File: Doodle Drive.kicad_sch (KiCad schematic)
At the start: 49 parts, among them J1 USB_B, J2 PINHD_1x4_Male, J6 PINHD_1x2_Male, SW1 Push_Button, SW2 Push_Button, SW3 Push_Button, U1 STM32F411RETx, U6 AP7343-30W5-7, U7 CP2102N-Axx-xQFN28, Y1 32.768KHz ±20ppm 12.5pF, Y2 25MHZ 9PF

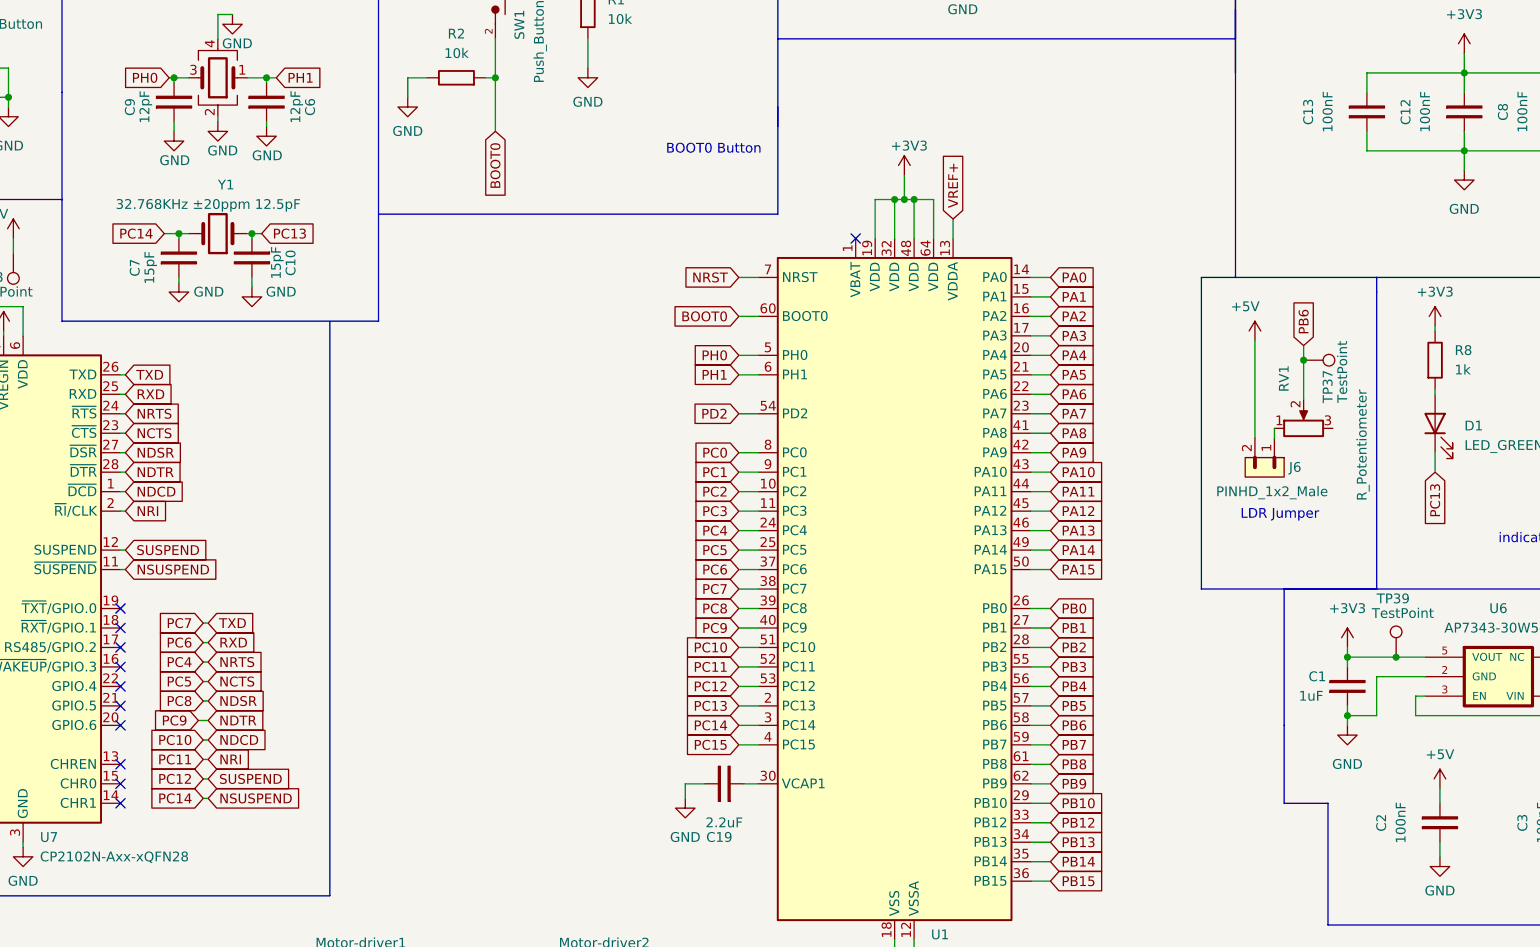
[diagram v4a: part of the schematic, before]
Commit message: deleted unnecessary testpoints
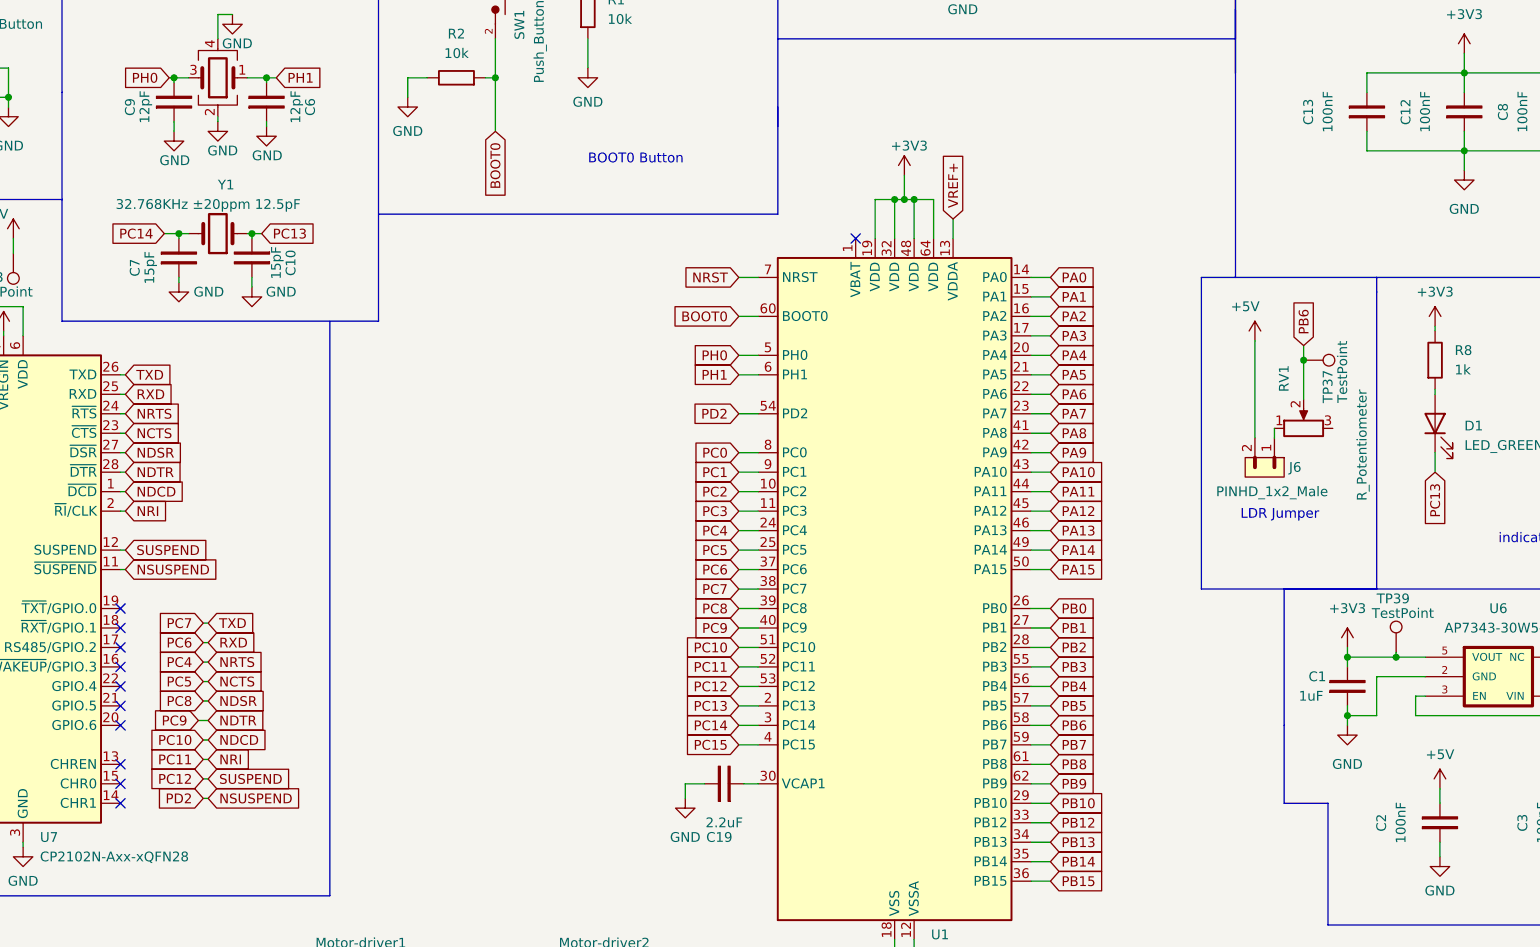
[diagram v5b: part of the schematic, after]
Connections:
- net PD2 is gone; now on net NSUSPEND: U1.54 (PD2)
- net NSUSPEND: no longer C7.2, U1.3 (PC14), Y1.2
- new net PC14: C7.2, U1.3 (PC14), Y1.2
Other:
- moved on the sheet: TP39
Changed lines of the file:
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@@
+    (stroke (width 0) (type default))
+  )
+  (wire (pts (xy 233.68 126.365) (xy 233.68 127))
     (stroke (width 0) (type default))
   )
@@
     (effects (font (size 1.27 1.27)) (justify left bottom))
   )
-  (text "BOOT0 Button" (at 138.43 61.595 0)
+  (text "BOOT0 Button" (at 128.27 62.865 0)
     (effects (font (size 1.27 1.27)) (justify left bottom))
   )
@@
     )
   )
-  (global_label "PC14" (shape input) (at 78.105 145.415 180) (fields_autoplaced)
-    (effects (font (size 1.27 1.27)) (justify right))
-    (property "Intersheetrefs" "${INTERSHEET_REFS}" (at 70.1608 145.415 0)
+  (global_label "PD2" (shape input) (at 78.105 145.415 180) (fields_autoplaced)
+    (effects (font (size 1.27 1.27)) (justify right))
+    (property "Intersheetrefs" "${INTERSHEET_REFS}" (at 71.3703 145.415 0)
       (effects (font (size 1.27 1.27)) (justify right) hide)
     )
@@
     )
   )
-  (symbol (lib_id "Connector:TestPoint") (at 233.68 127 0) (unit 1)
+  (symbol (lib_id "Connector:TestPoint") (at 233.68 126.365 0) (unit 1)
     (in_bom yes) (on_board yes) (dnp no)
     (property "Reference" "TP39" (at 231.14 119.38 0)
@@
       (effects (font (size 1.27 1.27)) (justify left))
     )
-    (property "Footprint" "TestPoint:TestPoint_Pad_D2.5mm" (at 238.76 127 0)
-      (effects (font (size 1.27 1.27)) hide)
-    )
-    (property "Datasheet" "~" (at 238.76 127 0)
-      (effects (font (size 1.27 1.27)) hide)
-    )
+    (property "Footprint" "TestPoint:TestPoint_Pad_D2.5mm" (at 238.76 126.365 0)
+      (effects (font (size 1.27 1.27)) hide)
+    )
+    (property "Datasheet" "~" (at 238.76 126.365 0)
+      (effects (font (size 1.27 1.27)) hide)
+    )

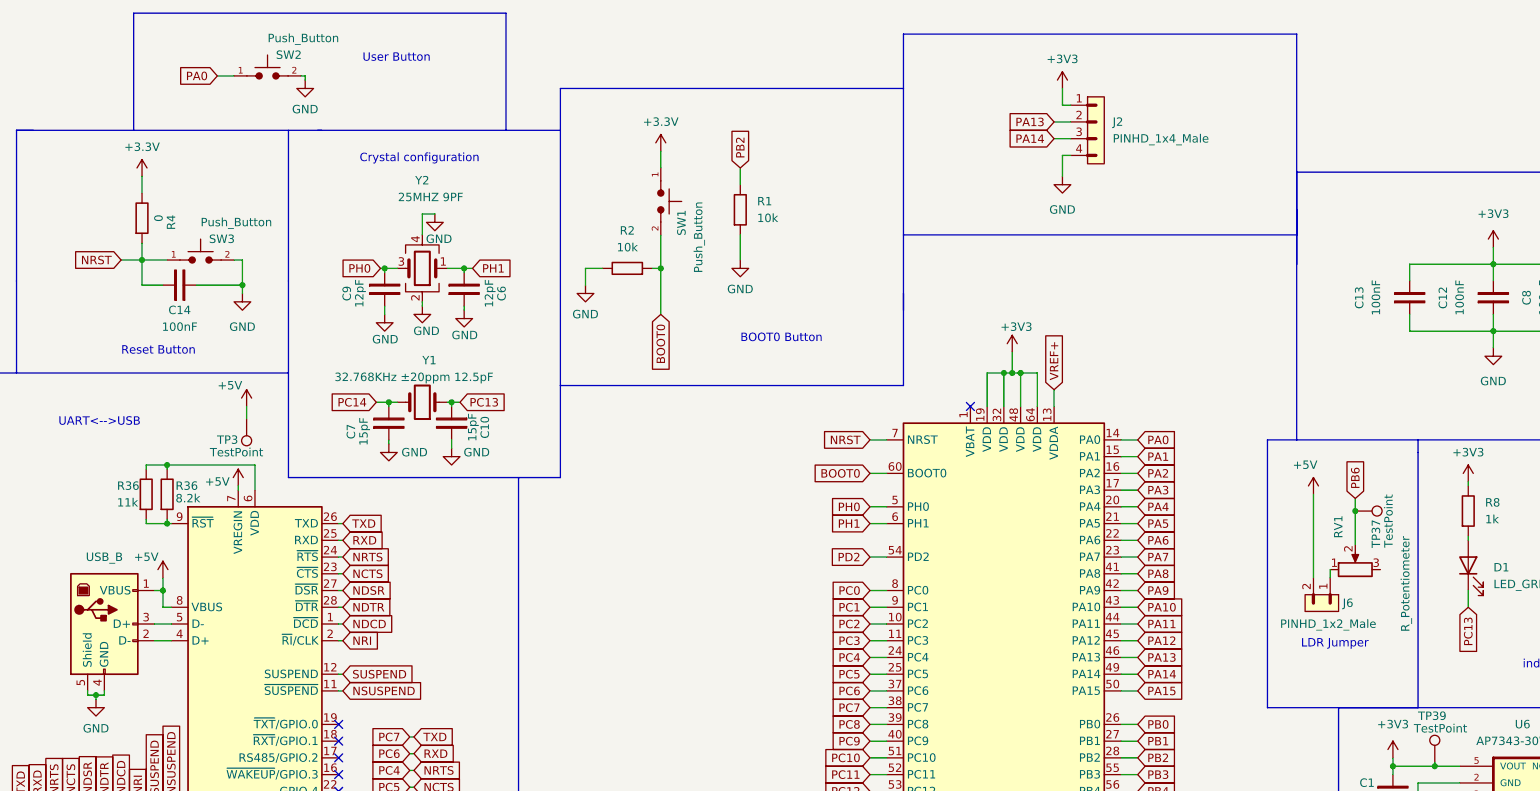
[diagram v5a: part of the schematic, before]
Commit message: fixed voltage dividers, roughly arrangenged components on pcb, set up 3V3 and GND area
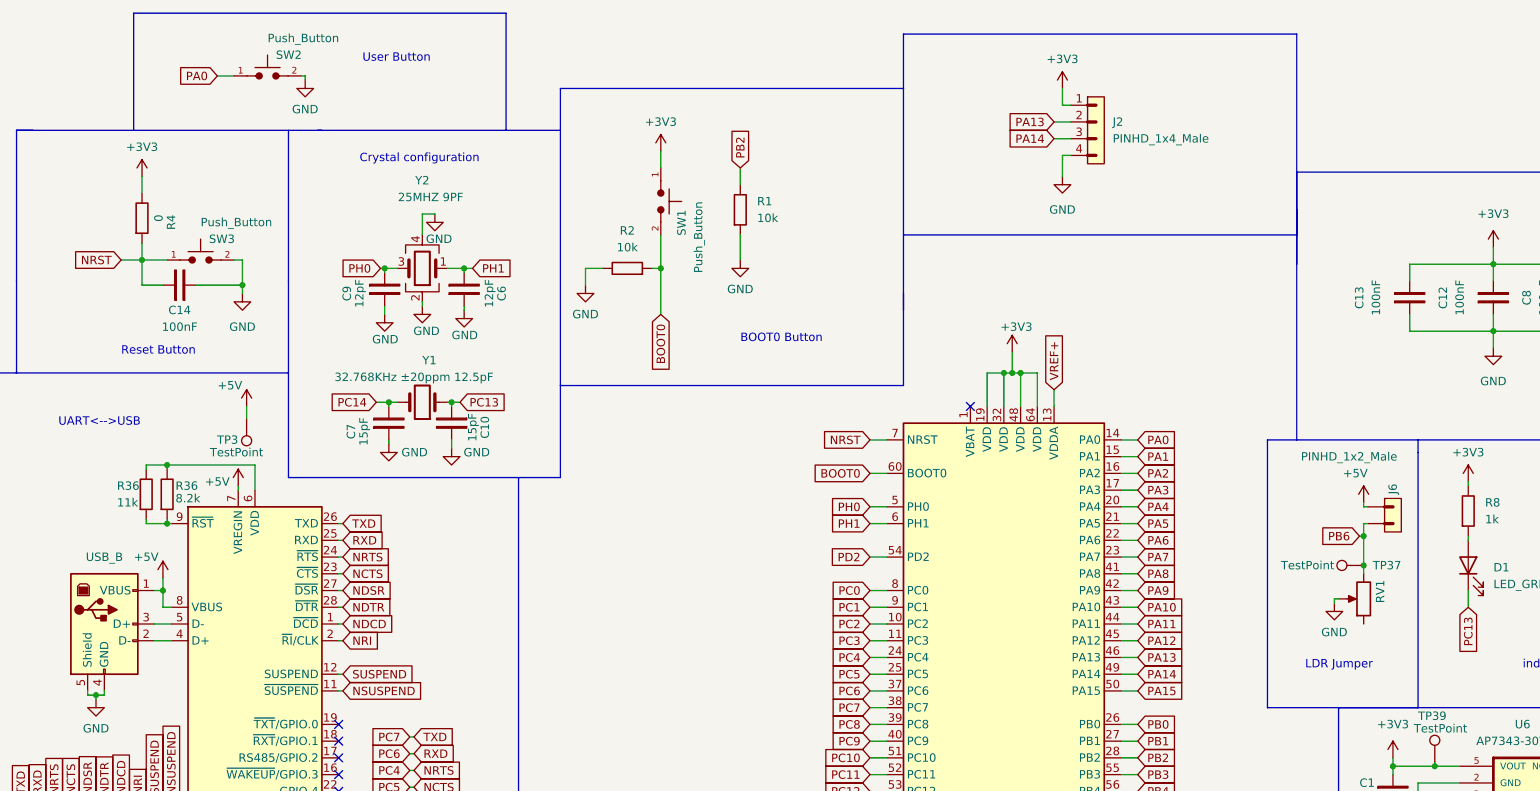
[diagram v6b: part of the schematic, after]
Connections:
- net +5V: now also J6.1; no longer J6.2
- net GND: now also RV1.2
- net PB6: now also J6.2, RV1.3; no longer RV1.2
- net at RV1.1: no longer J6.1
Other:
- moved on the sheet: TP37
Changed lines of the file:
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@@
   (junction (at 74.93 71.755) (diameter 0) (color 0 0 0 0)
   )
-  (junction (at 170.815 67.31) (diameter 0) (color 0 0 0 0)
+  (junction (at 222.885 96.52) (diameter 0) (color 0 0 0 0)
   )
-  (junction (at 221.615 88.265) (diameter 0) (color 0 0 0 0)
+  (junction (at 170.815 67.31) (diameter 0) (color 0 0 0 0)
   )
   (junction (at 255.27 60.96) (diameter 0) (color 0 0 0 0)
@@
   (junction (at 266.7 127) (diameter 0) (color 0 0 0 0)
   )
+  (junction (at 222.885 92.075) (diameter 0) (color 0 0 0 0)
+  )
   (junction (at 169.545 67.31) (diameter 0) (color 0 0 0 0)
   )
@@
     (stroke (width 0) (type default))
   )
-  (wire (pts (xy 217.805 98.425) (xy 217.805 97.155))
-    (stroke (width 0) (type default))
-  )
   (wire (pts (xy 186.055 102.87) (xy 188.595 102.87))
     (stroke (width 0) (type default))
@@
     (stroke (width 0) (type default))
   )
-  (wire (pts (xy 221.615 88.265) (xy 221.615 93.345))
-    (stroke (width 0) (type default))
-  )
   (wire (pts (xy 242.57 63.5) (xy 242.57 60.96))
     (stroke (width 0) (type default))
@@
     (stroke (width 0) (type default))
   )
+  (wire (pts (xy 222.885 87.63) (xy 222.885 86.995))
+    (stroke (width 0) (type default))
+  )
   (wire (pts (xy 256.54 132.08) (xy 257.81 132.08))
     (stroke (width 0) (type default))
@@
     (stroke (width 0) (type default))
   )
+  (wire (pts (xy 222.885 96.52) (xy 222.885 97.79))
+    (stroke (width 0) (type default))
+  )
   (wire (pts (xy 188.595 120.65) (xy 186.055 120.65))
     (stroke (width 0) (type default))
@@
     (stroke (width 0) (type default))
   )
+  (wire (pts (xy 222.885 90.17) (xy 222.885 92.075))
+    (stroke (width 0) (type default))
+  )
+  (wire (pts (xy 222.885 87.63) (xy 223.52 87.63))
+    (stroke (width 0) (type default))
+  )
   (wire (pts (xy 188.595 156.21) (xy 186.055 156.21))
     (stroke (width 0) (type default))
@@
     (stroke (width 0) (type default))
   )
-  (wire (pts (xy 215.265 98.425) (xy 215.265 85.725))
-    (stroke (width 0) (type default))
-  )
   (polyline (pts (xy 15.875 67.31) (xy 18.415 67.31))
     (stroke (width 0) (type default))
@@
     (stroke (width 0) (type default))
   )
+  (wire (pts (xy 222.885 90.17) (xy 223.52 90.17))
+    (stroke (width 0) (type default))
+  )
   (wire (pts (xy 233.68 126.365) (xy 233.68 127))
     (stroke (width 0) (type default))
@@
     (stroke (width 0) (type default))
   )
+  (wire (pts (xy 219.075 101.6) (xy 218.44 101.6))
+    (stroke (width 0) (type default))
+  )
   (polyline (pts (xy 231.14 79.375) (xy 231.14 118.11))
     (stroke (width 0) (type default))
@@
     (stroke (width 0) (type default))
   )
+  (wire (pts (xy 218.44 101.6) (xy 218.44 102.235))
+    (stroke (width 0) (type default))
+  )
   (wire (pts (xy 186.055 77.47) (xy 188.595 77.47))
     (stroke (width 0) (type default))
@@
     (stroke (width 0) (type default))
   )
+  (wire (pts (xy 222.885 92.075) (xy 222.885 96.52))
+    (stroke (width 0) (type default))
+  )
   (wire (pts (xy 168.275 67.31) (xy 169.545 67.31))
     (stroke (width 0) (type default))
@@
     (stroke (width 0) (type default))
   )
-  (wire (pts (xy 221.615 88.265) (xy 221.615 86.36))
+  (wire (pts (xy 188.595 135.89) (xy 186.055 135.89))
     (stroke (width 0) (type default))
   )
-  (wire (pts (xy 188.595 135.89) (xy 186.055 135.89))
+  (wire (pts (xy 222.25 92.075) (xy 222.885 92.075))
     (stroke (width 0) (type default))
   )
@@
     (effects (font (size 1.27 1.27)) (justify left bottom))
   )
-  (text "LDR Jumper" (at 213.36 109.22 0)
+  (text "LDR Jumper" (at 213.995 112.395 0)
     (effects (font (size 1.27 1.27)) (justify left bottom))
   )
@@
     )
   )
-  (global_label "PB6" (shape input) (at 221.615 86.36 90) (fields_autoplaced)
-    (effects (font (size 1.27 1.27)) (justify left))
-    (property "Intersheetrefs" "${INTERSHEET_REFS}" (at 221.615 79.6253 90)
-      (effects (font (size 1.27 1.27)) (justify left) hide)
+  (global_label "PB6" (shape input) (at 222.25 92.075 180) (fields_autoplaced)
+    (effects (font (size 1.27 1.27)) (justify right))
+    (property "Intersheetrefs" "${INTERSHEET_REFS}" (at 215.5153 92.075 0)
+      (effects (font (size 1.27 1.27)) (justify right) hide)
     )
   )
@@
     )
   )
-  (symbol (lib_id "PCM_SL_Pin_Headers:PINHD_1x2_Male") (at 216.535 102.235 270) (unit 1)
+  (symbol (lib_id "PCM_SL_Pin_Headers:PINHD_1x2_Male") (at 227.33 88.9 0) (unit 1)
     (in_bom yes) (on_board yes) (dnp no)
-    (property "Reference" "J6" (at 219.71 102.235 90)
+    (property "Reference" "J6" (at 227.33 85.725 90)
       (effects (font (size 1.27 1.27)) (justify left))
     )
-    (property "Value" "PINHD_1x2_Male" (at 210.185 105.41 90)
+    (property "Value" "PINHD_1x2_Male" (at 213.36 80.01 0)
       (effects (font (size 1.27 1.27)) (justify left))
     )
-    (property "Footprint" "Connector_PinHeader_2.54mm:PinHeader_1x02_P2.54mm_Vertical" (at 212.725 103.505 0)
+    (property "Footprint" "Connector_PinHeader_2.54mm:PinHeader_1x02_P2.54mm_Vertical" (at 228.6 92.71 0)
       (effects (font (size 1.27 1.27)) hide)
     )
-    (property "Datasheet" "" (at 224.155 102.235 0)
+    (property "Datasheet" "" (at 227.33 81.28 0)
       (effects (font (size 1.27 1.27)) hide)
     )
@@
     )
   )
-  (symbol (lib_id "power:+5V") (at 215.265 85.725 0) (unit 1)
+  (symbol (lib_id "power:+5V") (at 222.885 86.995 0) (unit 1)
     (in_bom yes) (on_board yes) (dnp no)
-    (property "Reference" "#PWR031" (at 215.265 89.535 0)
+    (property "Reference" "#PWR031" (at 222.885 90.805 0)
       (effects (font (size 1.27 1.27)) hide)
     )
-    (property "Value" "+5V" (at 213.995 81.28 0)
+    (property "Value" "+5V" (at 221.615 82.55 0)
       (effects (font (size 1.27 1.27)))
     )
-    (property "Footprint" "" (at 215.265 85.725 0)
+    (property "Footprint" "" (at 222.885 86.995 0)
       (effects (font (size 1.27 1.27)) hide)
     )
-    (property "Datasheet" "" (at 215.265 85.725 0)
+    (property "Datasheet" "" (at 222.885 86.995 0)
       (effects (font (size 1.27 1.27)) hide)
     )
@@
     )
   )
-  (symbol (lib_id "Connector:TestPoint") (at 221.615 88.265 270) (unit 1)
+  (symbol (lib_id "Connector:TestPoint") (at 222.885 96.52 90) (unit 1)
     (in_bom yes) (on_board yes) (dnp no)
-    (property "Reference" "TP37" (at 224.79 89.535 0)
+    (property "Reference" "TP37" (at 228.6 96.52 90)
       (effects (font (size 1.27 1.27)) (justify left))
     )
-    (property "Value" "TestPoint" (at 226.695 85.725 0)
+    (property "Value" "TestPoint" (at 218.44 96.52 90)
       (effects (font (size 1.27 1.27)) (justify left))
     )
-    (property "Footprint" "TestPoint:TestPoint_Pad_D2.5mm" (at 221.615 93.345 0)
+    (property "Footprint" "TestPoint:TestPoint_Pad_D2.5mm" (at 222.885 91.44 0)
       (effects (font (size 1.27 1.27)) hide)
     )
-    (property "Datasheet" "~" (at 221.615 93.345 0)
+    (property "Datasheet" "~" (at 222.885 91.44 0)
       (effects (font (size 1.27 1.27)) hide)
     )
@@
       (effects (font (size 1.27 1.27)) hide)
     )
-    (property "Value" "+3.3V" (at 37.465 33.02 0)
+    (property "Value" "+3V3" (at 37.465 33.02 0)
       (effects (font (size 1.27 1.27)))
     )
@@
       (effects (font (size 1.27 1.27)) hide)
     )
-    (property "Value" "+3.3V" (at 116.205 29.21 0)
+    (property "Value" "+3V3" (at 116.205 29.21 0)
       (effects (font (size 1.27 1.27)))
     )
@@
     )
   )
-  (symbol (lib_id "Device:R_Potentiometer") (at 221.615 97.155 90) (unit 1)
+  (symbol (lib_id "Device:R_Potentiometer") (at 222.885 101.6 180) (unit 1)
     (in_bom yes) (on_board yes) (dnp no)
-    (property "Reference" "RV1" (at 219.075 88.9 0)
+    (property "Reference" "RV1" (at 225.425 102.235 90)
       (effects (font (size 1.27 1.27)) (justify right))
     )
-    (property "Value" "R_Potentiometer" (at 229.235 92.075 0)
-      (effects (font (size 1.27 1.27)) (justify right))
+    (property "Value" "R_Potentiometer" (at 217.805 93.98 0)
+      (effects (font (size 1.27 1.27)) (justify right) hide)
     )
-    (property "Footprint" "Potentiometer_THT:Potentiometer_ACP_CA6-H2,5_Horizontal" (at 221.615 97.155 0)
+    (property "Footprint" "Potentiometer_THT:Potentiometer_ACP_CA6-H2,5_Horizontal" (at 222.885 101.6 0)
       (effects (font (size 1.27 1.27)) hide)
     )
-    (property "Datasheet" "~" (at 221.615 97.155 0)
+    (property "Datasheet" "~" (at 222.885 101.6 0)
       (effects (font (size 1.27 1.27)) hide)
     )
@@
         )
       )
+    )
+  )
+  (symbol (lib_id "power:GND") (at 218.44 102.235 0) (unit 1)
+    (in_bom yes) (on_board yes) (dnp no) (fields_autoplaced)
+    (property "Reference" "#PWR057" (at 218.44 108.585 0)
+      (effects (font (size 1.27 1.27)) hide)
+    )
+    (property "Value" "GND" (at 218.44 106.68 0)
+      (effects (font (size 1.27 1.27)))
+    )
+    (property "Footprint" "" (at 218.44 102.235 0)
+      (effects (font (size 1.27 1.27)) hide)
+    )
+    (property "Datasheet" "" (at 218.44 102.235 0)
+      (effects (font (size 1.27 1.27)) hide)
+    )
+    (pin "1")
+    (instances
+      (project "Doodle Drive"
+        (path "/3ec634aa-8c09-482d-9325-2288a4dbd68b"
+          (reference "#PWR057") (unit 1)
+        )
+      )
